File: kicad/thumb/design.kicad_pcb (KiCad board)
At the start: 2 copper layers, 99.1 x 41.3 mm, 13 parts, among them P2 CONN_6, SW1 SW_00, SW10 SW_10, SW11 SW_21, SW15 SW_20, SW2 SW_01, SW6 SW_11

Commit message: working on thumb cluster
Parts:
- added D3: DIODE, SM1206POL, F.Cu at (59.7, 59.7)
- added D4: DIODE, SM1206POL, F.Cu at (43.8, 52.7)
- added D5: DIODE, SM1206POL, F.Cu at (34.9, 36.2)
- added D7: DIODE, SM1206POL, F.Cu at (40.6, 62.2)
- added P1: CONN_1, 1pin, F.Cu at (69.2, 67.9)
- added P3: CONN_1, 1pin, F.Cu at (69.2, 29.8)
- added P4: CONN_1, 1pin, F.Cu at (29.8, 29.8)
- added SW3: SW_21, SW_PCB_2PIN, B.Cu at (68.7, 54.9)
- added SW4: SW_11, SW_PCB_2PIN, B.Cu at (50.2, 60.7)
- added SW5: SW_10, SW_PCB_2PIN, B.Cu at (40.8, 44.2)
- added SW7: SW_01, SW_PCB_2PIN, B.Cu at (30.6, 65.2)
- D1: moved to F.Cu
- SW1: value SW_00 -> SW_20; moved to B.Cu
- moved SW1 28.2 mm to (59.3, 38.6), turned to 210 degrees
- moved D1 25.4 mm to (52.7, 31.1), turned to 0 degrees
- moved D15 21.2 mm to (52.7, 31.1)
- moved D10 17.3 mm to (34.9, 36.2)
- moved D6 12.5 mm to (43.8, 52.7)
- moved SW10 11.2 mm to (40.8, 44.2), turned to 30 degrees
- moved D11 10.3 mm to (59.7, 59.7), turned to 270 degrees
- moved SW15 9.92 mm to (59.3, 38.6), turned to 30 degrees
- moved D2 9.61 mm to (40.6, 62.2), turned to 90 degrees
- moved SW2 8.02 mm to (30.6, 65.2), turned to 300 degrees
- moved SW6 3.56 mm to (50.2, 60.7), turned to 30 degrees
- moved SW11 2.34 mm to (68.7, 54.9), turned to 120 degrees
- moved P2 2.01 mm to (48.3, 27.3)
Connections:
- D1 pad 2: R0 -> (no net)
- P2 pad 2: C2 -> C0
- P2 pad 4: C0 -> C2
- SW1 pad 2: C0 -> C2
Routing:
- net R1: track 0.00 -> 104.6 mm, vias 0 -> 2
- net C0: track 0.00 -> 56.1 mm
- net C1: track 0.00 -> 52.0 mm
- net C2: track 0.00 -> 51.4 mm
- net R0: track 0.00 -> 28.2 mm, vias 0 -> 2
- net N-000003: track 0.00 -> 6.97 mm
- net N-000004: track 0.00 -> 6.92 mm
- net N-000008: track 0.00 -> 6.78 mm
- net N-000005: track 0.00 -> 6.61 mm
- net N-000006: track 0.00 -> 6.22 mm
- net N-0000016: track 0.00 -> 5.74 mm
- net N-0000017: track 0.00 -> 5.56 mm
- net N-0000014: track 0.00 -> 5.40 mm
- net N-0000015: track 0.00 -> 4.75 mm
- net N-0000013: track 0.00 -> 4.52 mm
- added copper zone on B.Cu, net GND
- added copper zone on F.Cu, net GND
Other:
- board size 99.1 x 41.3 mm -> 48.3 x 47 mm
- net class Default: trace_width 0.254 -> 0.508
- net class Seeed added: clearance 0.254, trace_width 0.508, via_dia 0.889, via_drill 0.635

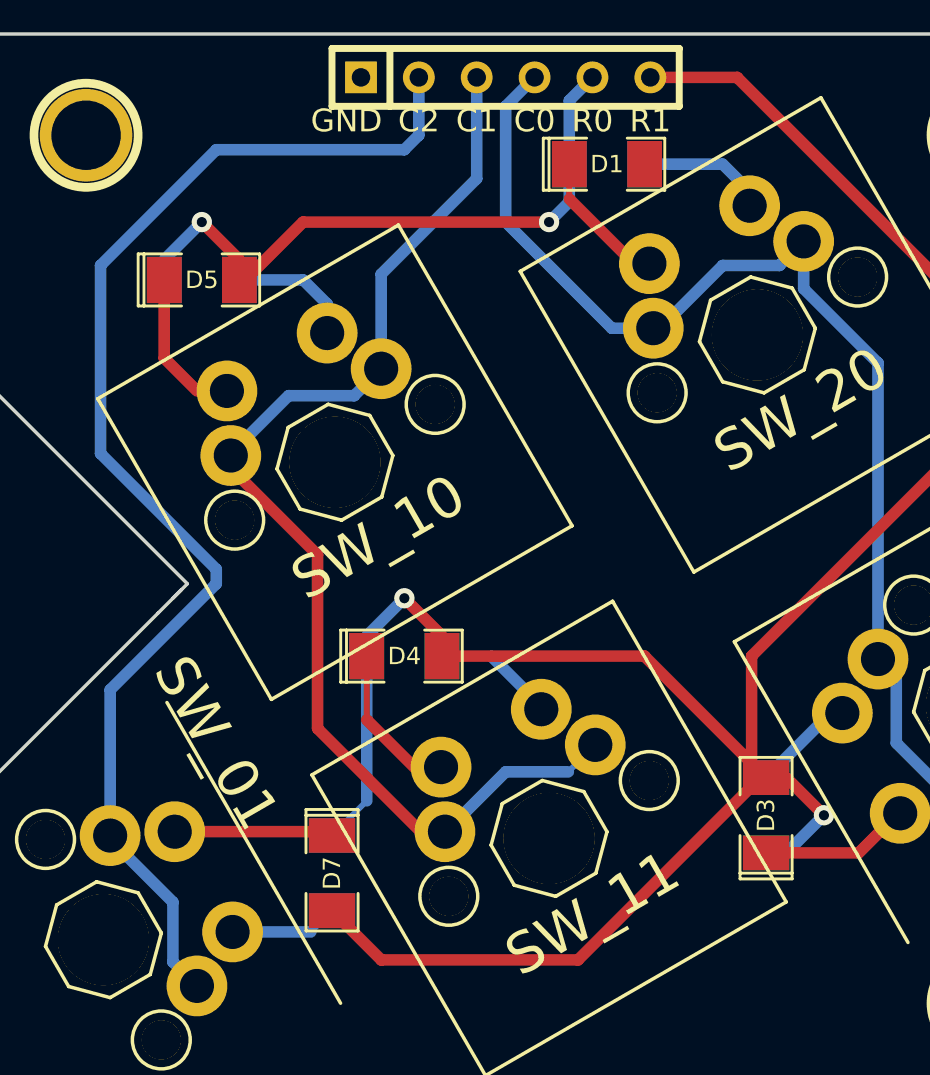
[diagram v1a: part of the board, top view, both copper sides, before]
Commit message: reversing all of the diodes
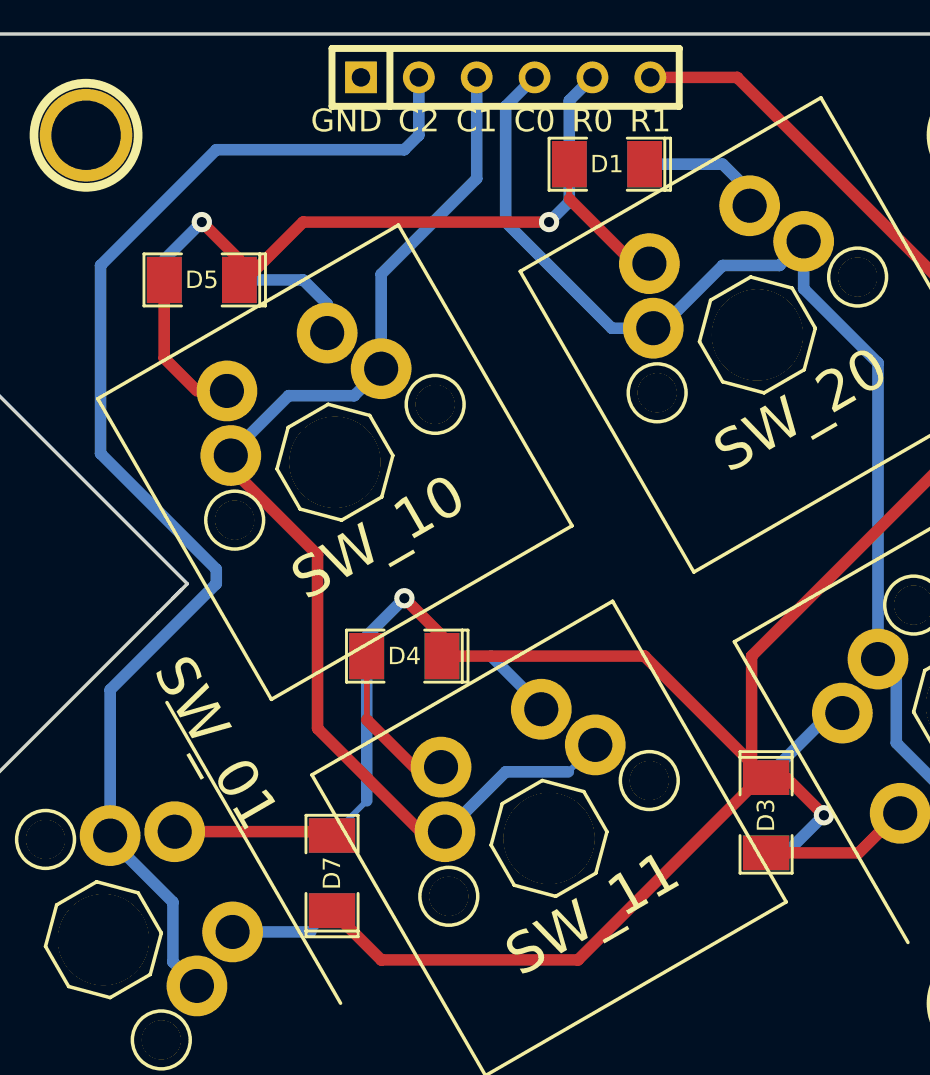
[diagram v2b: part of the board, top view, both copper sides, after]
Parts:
- turned D1 to 180 degrees
- turned D10 to 0 degrees
- turned D11 to 90 degrees
- turned D15 to 0 degrees
- turned D2 to 270 degrees
- turned D3 to 270 degrees
- turned D4 to 180 degrees
- turned D5 to 180 degrees
- turned D6 to 0 degrees
- turned D7 to 90 degrees
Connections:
- D1 pad 1: N-000006 -> (no net)
- D1 pad 2: (no net) -> N-000006
- D10 pad 1: N-0000017 -> R0
- D10 pad 2: R0 -> N-0000017
- D11 pad 1: N-0000013 -> R1
- D11 pad 2: R1 -> N-0000013
- D15 pad 1: N-0000016 -> R0
- D15 pad 2: R0 -> N-0000016
- D2 pad 1: N-0000015 -> R1
- D2 pad 2: R1 -> N-0000015
- D3 pad 1: N-000005 -> R1
- D3 pad 2: R1 -> N-000005
- D4 pad 1: N-000004 -> R1
- D4 pad 2: R1 -> N-000004
- D5 pad 1: N-000008 -> R0
- D5 pad 2: R0 -> N-000008
- D6 pad 1: N-0000014 -> R1
- D6 pad 2: R1 -> N-0000014
- D7 pad 1: N-000003 -> R1
- D7 pad 2: R1 -> N-000003

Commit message: generated output for seeedstudio order
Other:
- board text added: "C0_9"
- board text added: "C1_8"
- board text added: "C2_7"
- board text added: "R5"
- board text added: "R6"
- board text added: "Warren Janssens"
- board text removed: "C0"
- board text removed: "C1"
- board text removed: "C2"
- board text removed: "R0"
- board text removed: "R1"
